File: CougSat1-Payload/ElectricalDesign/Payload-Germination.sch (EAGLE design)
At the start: 7 parts, among them J1 CougSat Socket, Q1 CSD25402Q3A, Q2 CSD25402Q3A, U1 TXS0102DQM, U2 TXS0102DQM, U3 TXS0102DQM

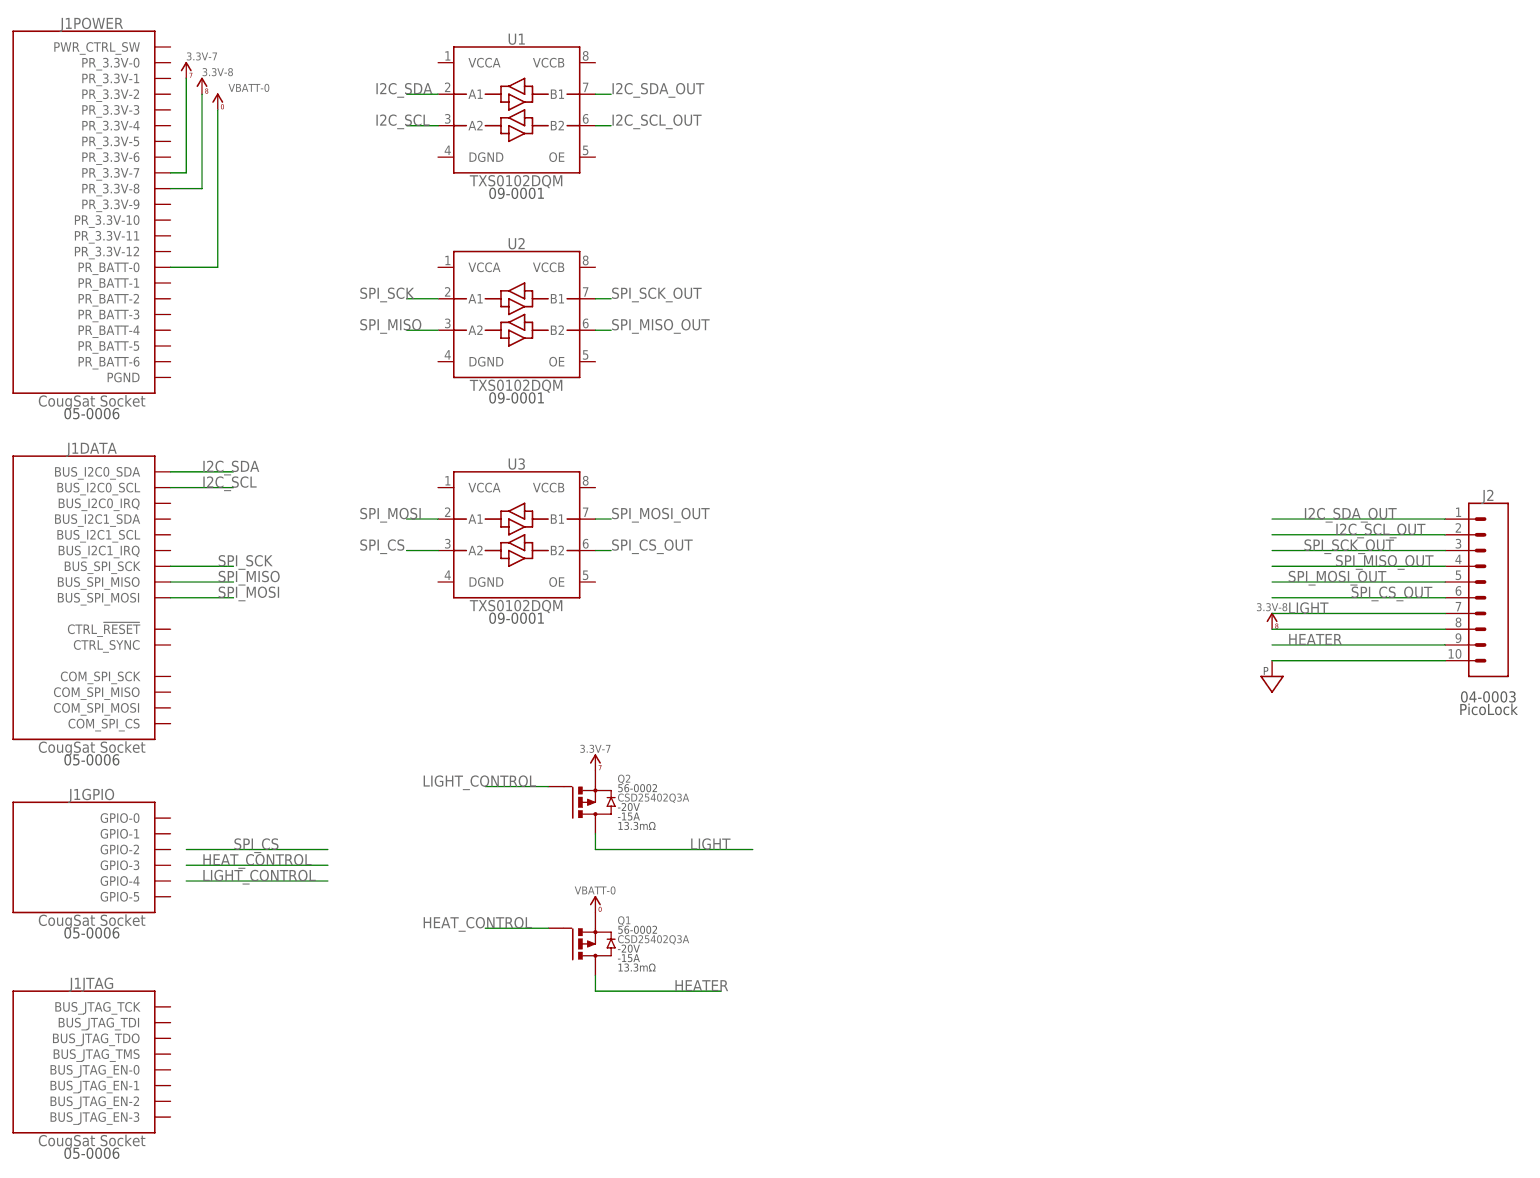
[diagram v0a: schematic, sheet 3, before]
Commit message: Completed Schematic
Fixes #185
Added powerlines to buffers
Labeled aesthetics in&out to appropriate data lines.
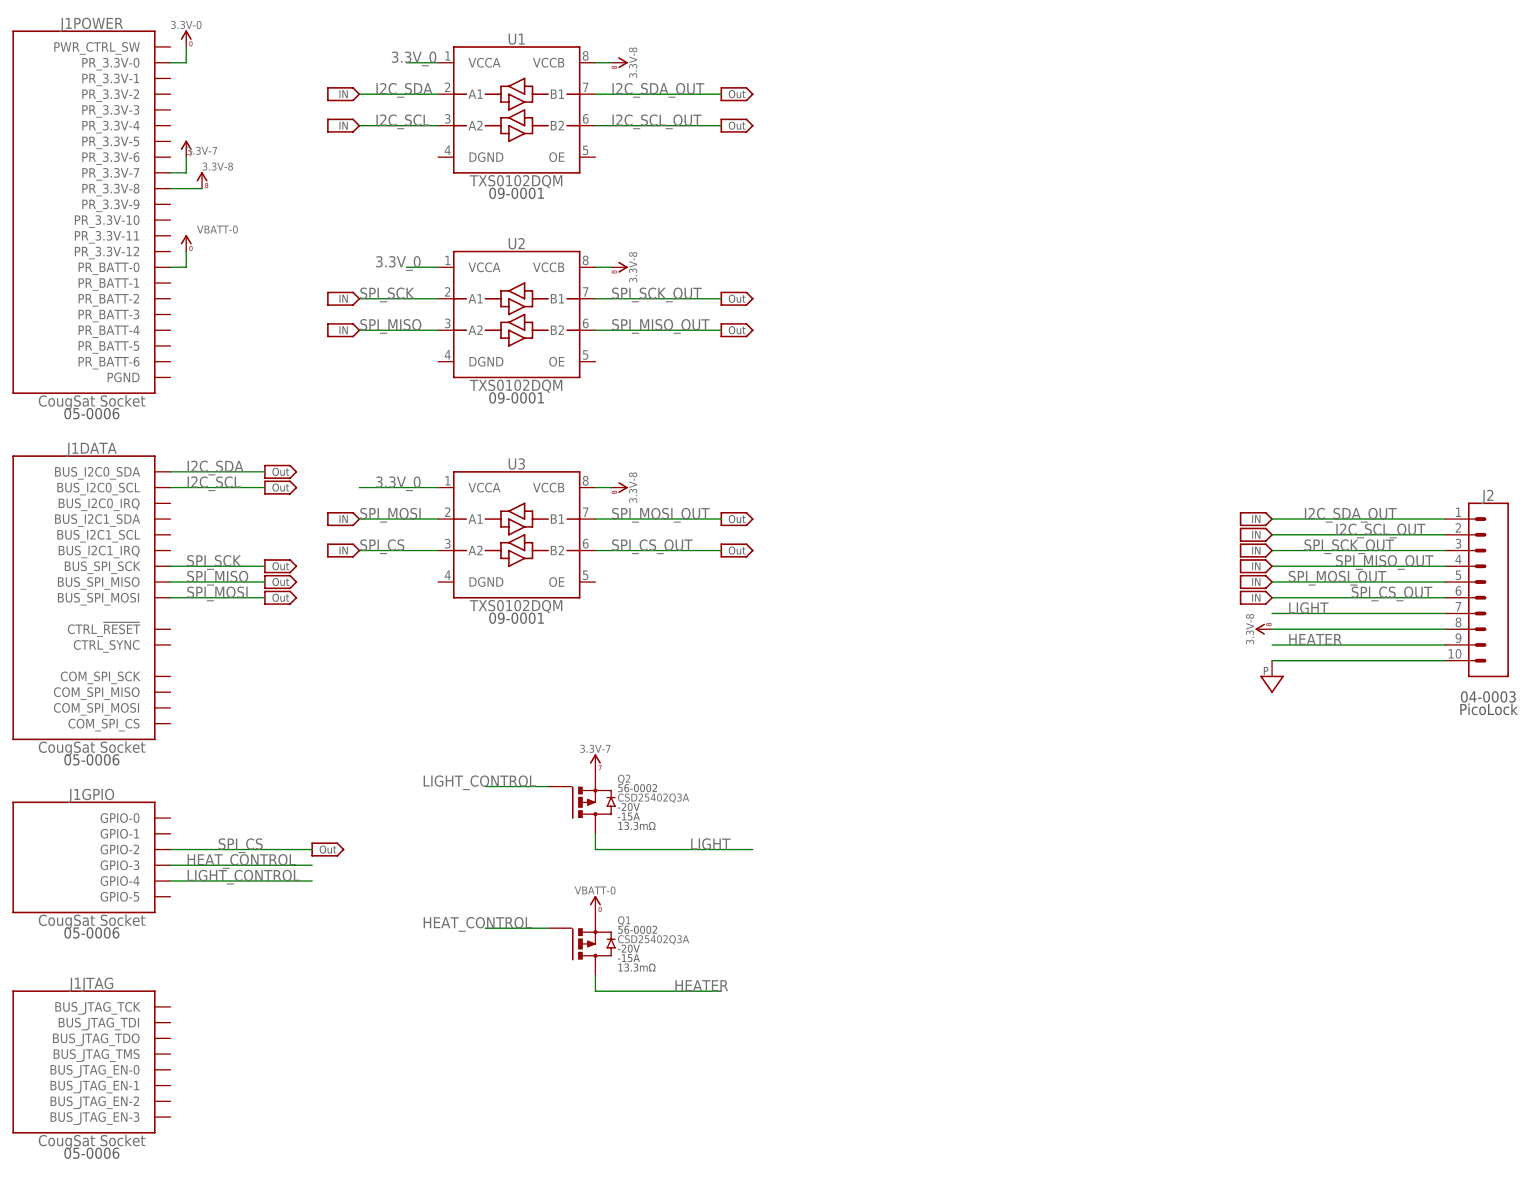
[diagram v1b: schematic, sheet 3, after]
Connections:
- new net 3.3V_0: J1POWER.PR_3.3V-0, U1.VCCA, U2.VCCA, U3.VCCA
- net 3.3V_8: now also U1.VCCB, U2.VCCB, U3.VCCB
- net HEAT_CONTROL: now also J1GPIO.GPIO-3
- net LIGHT_CONTROL: now also J1GPIO.GPIO-4
- net SPI_CS: now also J1GPIO.GPIO-2
